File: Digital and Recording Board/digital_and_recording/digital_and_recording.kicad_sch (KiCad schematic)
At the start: 0 parts

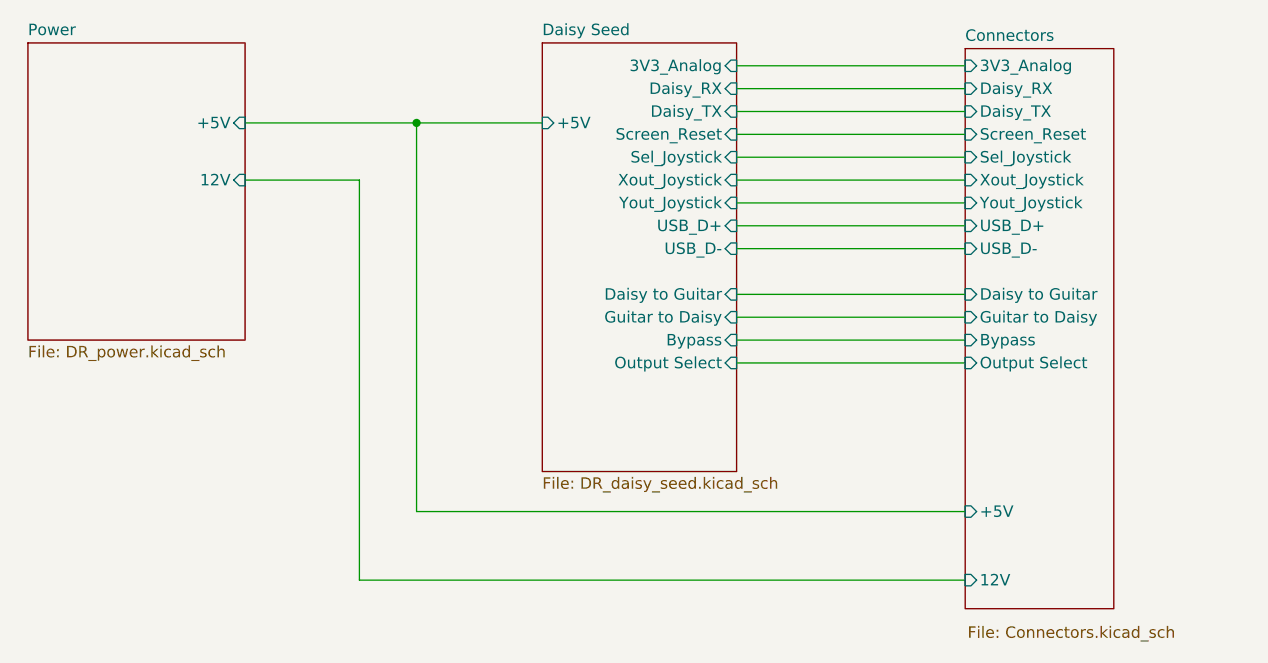
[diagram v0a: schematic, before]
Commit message: updated schematic to use +/-5 DCDC
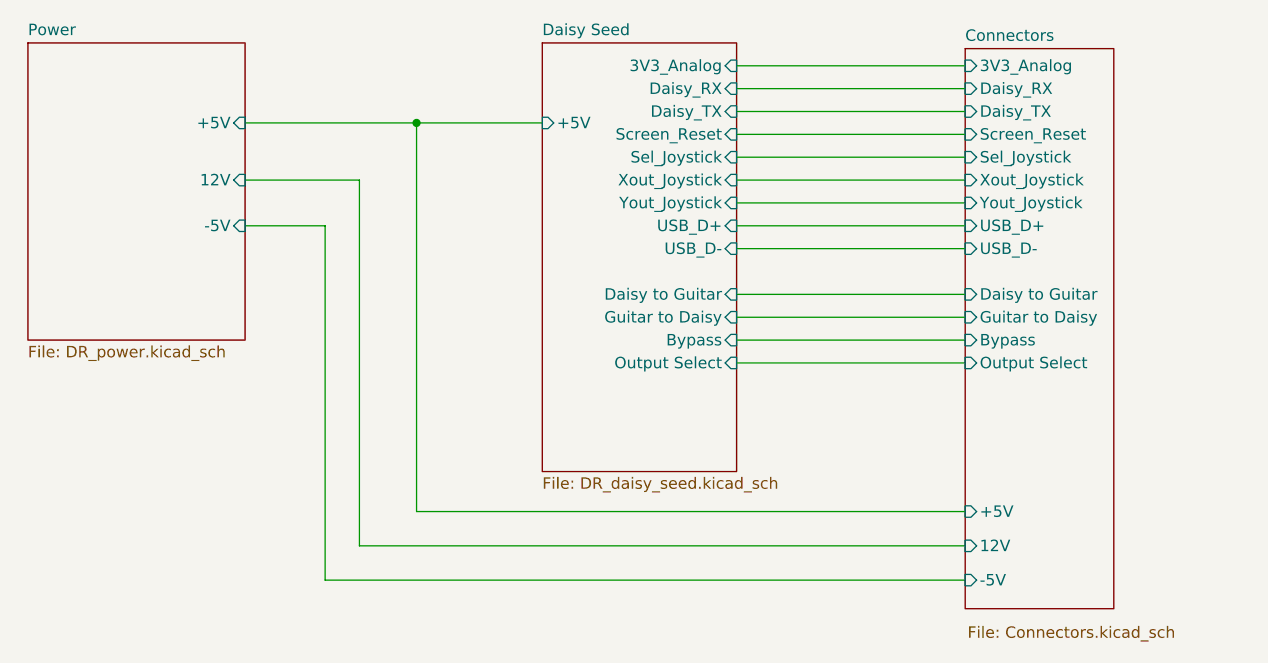
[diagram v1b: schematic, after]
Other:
- sheet Connectors ports: added -5V; removed none
- sheet Power ports: added -5V; removed none
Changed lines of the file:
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@@
+	(wire
+		(pts
+			(xy 113.03 85.09) (xy 113.03 125.73)
+		)
+		(stroke
+			(width 0)
+			(type default)
+		)
+	)
 	(wire
 		(pts
@@
 	(wire
 		(pts
-			(xy 113.03 85.09) (xy 113.03 129.54)
-		)
-		(stroke
-			(width 0)
-			(type default)
-		)
-	)
-	(wire
-		(pts
 			(xy 154.94 92.71) (xy 180.34 92.71)
 		)
@@
 	(wire
 		(pts
+			(xy 113.03 125.73) (xy 180.34 125.73)
+		)
+		(stroke
+			(width 0)
+			(type default)
+		)
+	)
+	(wire
+		(pts
 			(xy 154.94 77.47) (xy 180.34 77.47)
 		)
@@
 	(wire
 		(pts
-			(xy 113.03 129.54) (xy 180.34 129.54)
-		)
-		(stroke
-			(width 0)
-			(type default)
-		)
-	)
-	(wire
-		(pts
 			(xy 119.38 78.74) (xy 119.38 121.92)
 		)
@@
 	(wire
 		(pts
+			(xy 109.22 129.54) (xy 180.34 129.54)
+		)
+		(stroke
+			(width 0)
+			(type default)
+		)
+	)
+	(wire
+		(pts
 			(xy 119.38 78.74) (xy 133.35 78.74)
 		)
@@
 	(wire
 		(pts
+			(xy 100.33 90.17) (xy 109.22 90.17)
+		)
+		(stroke
+			(width 0)
+			(type default)
+		)
+	)
+	(wire
+		(pts
 			(xy 154.94 105.41) (xy 180.34 105.41)
 		)
@@
 		(pts
 			(xy 154.94 82.55) (xy 180.34 82.55)
+		)
+		(stroke
+			(width 0)
+			(type default)
+		)
+	)
+	(wire
+		(pts
+			(xy 109.22 90.17) (xy 109.22 129.54)
 		)
 		(stroke
@@
 			)
 		)
+		(pin "-5V" input
+			(at 100.33 90.17 0)
+			(effects
+				(font
+					(size 1.27 1.27)
+				)
+				(justify right)
+			)
+		)
 		(instances
 			(project "digital_and_recording"
@@
 		)
 		(pin "12V" input
-			(at 180.34 129.54 180)
+			(at 180.34 125.73 180)
 			(effects
 				(font
@@
 			(effects
 				(font
+					(size 1.27 1.27)
+				)
+				(justify left)
+			)
+		)
+		(pin "-5V" input
+			(at 180.34 129.54 180)
+			(effects
+				(font

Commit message: modified power for proper amp rating of daisy seed
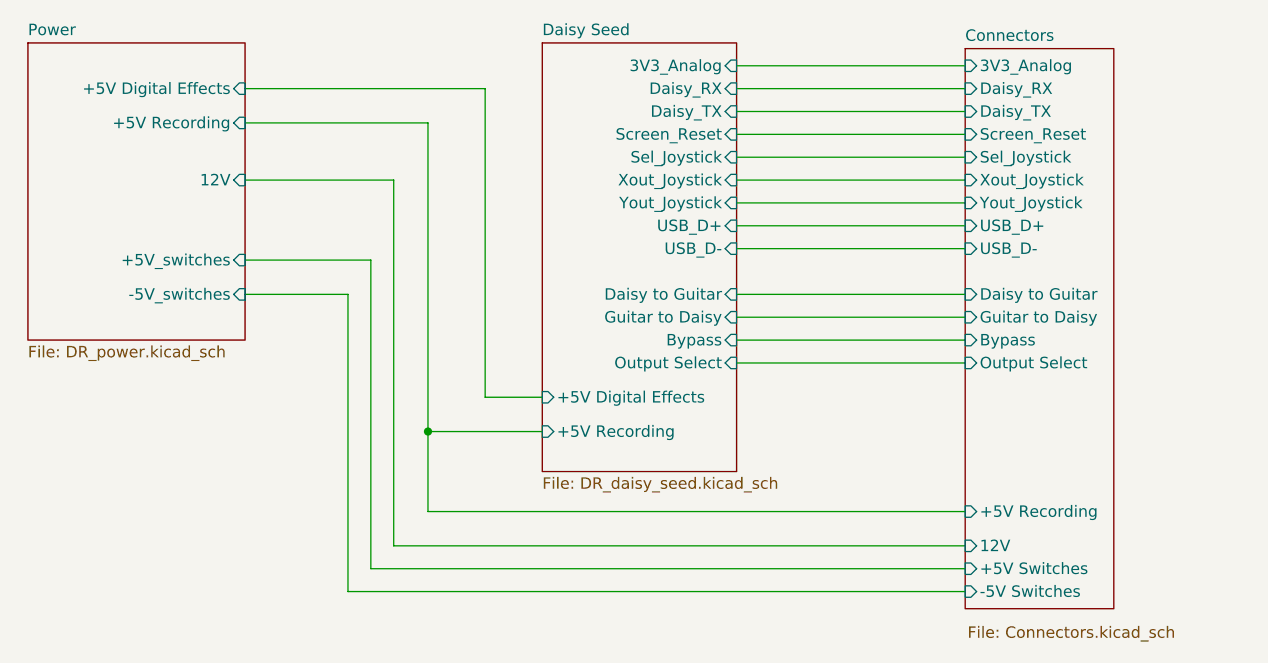
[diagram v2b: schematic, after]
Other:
- sheet Connectors ports: added +5V Recording, +5V Switches, -5V Switches; removed +5V, -5V
- sheet Daisy Seed ports: added +5V Digital Effects, +5V Recording; removed +5V
- sheet Power ports: added +5V Digital Effects, +5V Recording, +5V_switches, -5V_switches; removed +5V, -5V
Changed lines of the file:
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@@
 	)
 	(junction
-		(at 119.38 78.74)
+		(at 120.65 113.03)
 		(diameter 0)
 		(color 0 0 0 0)
@@
 	(wire
 		(pts
-			(xy 113.03 85.09) (xy 113.03 125.73)
-		)
-		(stroke
-			(width 0)
-			(type default)
-		)
-	)
-	(wire
-		(pts
-			(xy 113.03 85.09) (xy 100.33 85.09)
+			(xy 100.33 85.09) (xy 116.84 85.09)
 		)
 		(stroke
@@
 	(wire
 		(pts
+			(xy 127 109.22) (xy 133.35 109.22)
+		)
+		(stroke
+			(width 0)
+			(type default)
+		)
+	)
+	(wire
+		(pts
 			(xy 154.94 85.09) (xy 180.34 85.09)
 		)
@@
 	(wire
 		(pts
+			(xy 180.34 121.92) (xy 120.65 121.92)
+		)
+		(stroke
+			(width 0)
+			(type default)
+		)
+	)
+	(wire
+		(pts
+			(xy 111.76 130.81) (xy 180.34 130.81)
+		)
+		(stroke
+			(width 0)
+			(type default)
+		)
+	)
+	(wire
+		(pts
 			(xy 154.94 92.71) (xy 180.34 92.71)
 		)
@@
 	(wire
 		(pts
-			(xy 113.03 125.73) (xy 180.34 125.73)
+			(xy 116.84 85.09) (xy 116.84 125.73)
 		)
 		(stroke
@@
 	(wire
 		(pts
-			(xy 119.38 78.74) (xy 119.38 121.92)
-		)
-		(stroke
-			(width 0)
-			(type default)
-		)
-	)
-	(wire
-		(pts
-			(xy 109.22 129.54) (xy 180.34 129.54)
-		)
-		(stroke
-			(width 0)
-			(type default)
-		)
-	)
-	(wire
-		(pts
-			(xy 119.38 78.74) (xy 133.35 78.74)
+			(xy 111.76 97.79) (xy 111.76 130.81)
+		)
+		(stroke
+			(width 0)
+			(type default)
+		)
+	)
+	(wire
+		(pts
+			(xy 120.65 121.92) (xy 120.65 113.03)
+		)
+		(stroke
+			(width 0)
+			(type default)
+		)
+	)
+	(wire
+		(pts
+			(xy 127 74.93) (xy 127 109.22)
 		)
 		(stroke
@@
 	(wire
 		(pts
+			(xy 114.3 128.27) (xy 180.34 128.27)
+		)
+		(stroke
+			(width 0)
+			(type default)
+		)
+	)
+	(wire
+		(pts
+			(xy 100.33 97.79) (xy 111.76 97.79)
+		)
+		(stroke
+			(width 0)
+			(type default)
+		)
+	)
+	(wire
+		(pts
 			(xy 154.94 102.87) (xy 180.34 102.87)
 		)
@@
 	(wire
 		(pts
+			(xy 116.84 125.73) (xy 180.34 125.73)
+		)
+		(stroke
+			(width 0)
+			(type default)
+		)
+	)
+	(wire
+		(pts
 			(xy 154.94 74.93) (xy 180.34 74.93)
 		)
@@
 	(wire
 		(pts
-			(xy 100.33 90.17) (xy 109.22 90.17)
-		)
-		(stroke
-			(width 0)
-			(type default)
-		)
-	)
-	(wire
-		(pts
 			(xy 154.94 105.41) (xy 180.34 105.41)
 		)
@@
 	(wire
 		(pts
-			(xy 119.38 121.92) (xy 180.34 121.92)
-		)
-		(stroke
-			(width 0)
-			(type default)
-		)
-	)
-	(wire
-		(pts
-			(xy 100.33 78.74) (xy 119.38 78.74)
+			(xy 120.65 113.03) (xy 133.35 113.03)
 		)
 		(stroke
@@
 	(wire
 		(pts
-			(xy 109.22 90.17) (xy 109.22 129.54)
+			(xy 114.3 93.98) (xy 114.3 128.27)
+		)
+		(stroke
+			(width 0)
+			(type default)
+		)
+	)
+	(wire
+		(pts
+			(xy 120.65 78.74) (xy 120.65 113.03)
+		)
+		(stroke
+			(width 0)
+			(type default)
+		)
+	)
+	(wire
+		(pts
+			(xy 100.33 74.93) (xy 127 74.93)
+		)
+		(stroke
+			(width 0)
+			(type default)
+		)
+	)
+	(wire
+		(pts
+			(xy 100.33 78.74) (xy 120.65 78.74)
+		)
+		(stroke
+			(width 0)
+			(type default)
+		)
+	)
+	(wire
+		(pts
+			(xy 100.33 93.98) (xy 114.3 93.98)
 		)
 		(stroke
@@
 			)
 		)
-		(pin "+5V" input
-			(at 100.33 78.74 0)
-			(effects
-				(font
-					(size 1.27 1.27)
-				)
-				(justify right)
-			)
-		)
 		(pin "12V" input
 			(at 100.33 85.09 0)
@@
 			)
 		)
-		(pin "-5V" input
-			(at 100.33 90.17 0)
+		(pin "+5V Digital Effects" input
+			(at 100.33 74.93 0)
+			(effects
+				(font
+					(size 1.27 1.27)
+				)
+				(justify right)
+			)
+		)
+		(pin "+5V Recording" input
+			(at 100.33 78.74 0)
+			(effects
+				(font
+					(size 1.27 1.27)
+				)
+				(justify right)
+			)
+		)
+		(pin "+5V_switches" input
+			(at 100.33 93.98 0)
+			(effects
+				(font
+					(size 1.27 1.27)
+				)
+				(justify right)
+			)
+		)
+		(pin "-5V_switches" input
+			(at 100.33 97.79 0)
 			(effects
 				(font
@@
 			)
 		)
-		(pin "+5V" input
-			(at 133.35 78.74 180)
-			(effects
-				(font
-					(size 1.27 1.27)
-				)
-				(justify left)
-			)
-		)
 		(pin "3V3_Analog" input
 			(at 154.94 72.39 0)
@@
 				)
 				(justify right)
+			)
+		)
+		(pin "+5V Digital Effects" input
+			(at 133.35 109.22 180)
+			(effects
+				(font
+					(size 1.27 1.27)
+				)
+				(justify left)
+			)
+		)
+		(pin "+5V Recording" input
+			(at 133.35 113.03 180)
+			(effects
+				(font
+					(size 1.27 1.27)
+				)
+				(justify left)
 			)
 		)
@@
 			)
 		)
-		(pin "+5V" input
-			(at 180.34 121.92 180)
-			(effects
-				(font
-					(size 1.27 1.27)
-				)
-				(justify left)
-			)
-		)
 		(pin "3V3_Analog" input
 			(at 180.34 72.39 180)
@@
 			)
 		)
-		(pin "-5V" input
-			(at 180.34 129.54 180)
-			(effects
-				(font
+		(pin "+5V Recording" input
+			(at 180.34 121.92 180)
+			(effects
+				(font
+					(size 1.27 1.27)
+				)
+				(justify left)
+			)
+		)
+		(pin "+5V Switches" input
+			(at 180.34 128.27 180)
+			(effects
+				(font
+					(size 1.27 1.27)
+				)
+				(justify left)
+			)
+		)
+		(pin "-5V Switches" input
+			(at 180.34 130.81 180)
+			(effects
+				(font

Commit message: updated schematic of digital and recording board to use 2 pin molex for power and guitar signals
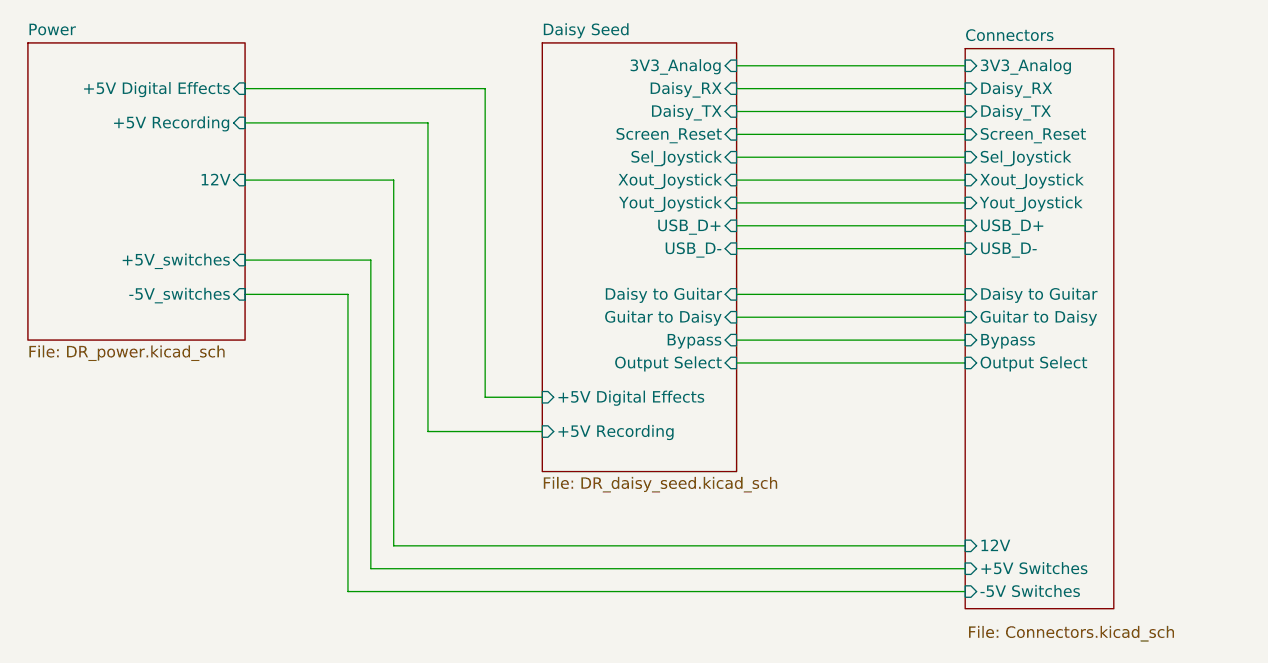
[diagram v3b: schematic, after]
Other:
- sheet Connectors ports: added none; removed +5V Recording
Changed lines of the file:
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@@
 		(company "RGA")
 	)
-	(junction
-		(at 120.65 113.03)
-		(diameter 0)
-		(color 0 0 0 0)
-	)
 	(wire
 		(pts
@@
 	(wire
 		(pts
-			(xy 180.34 121.92) (xy 120.65 121.92)
-		)
-		(stroke
-			(width 0)
-			(type default)
-		)
-	)
-	(wire
-		(pts
 			(xy 111.76 130.81) (xy 180.34 130.81)
 		)
@@
 		(pts
 			(xy 111.76 97.79) (xy 111.76 130.81)
-		)
-		(stroke
-			(width 0)
-			(type default)
-		)
-	)
-	(wire
-		(pts
-			(xy 120.65 121.92) (xy 120.65 113.03)
 		)
 		(stroke
@@
 			(effects
 				(font
-					(size 1.27 1.27)
-				)
-				(justify left)
-			)
-		)
-		(pin "+5V Recording" input
-			(at 180.34 121.92 180)
-			(effects
-				(font
